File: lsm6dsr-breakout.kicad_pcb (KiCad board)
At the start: 2 copper layers, 16.5 x 20.3 mm, 16 parts, among them CN1 AFC10-S04QCA-00, CN2 AFC10-S04QCA-00, J1 Conn_01x06_Pin, J2 Conn_01x04_Pin, U1 LSM6DSRTR

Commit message: beautify schematic
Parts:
- removed the R1 at (56.0, 46.2)
- removed the R1 at (60.3, 51.8)
- added R1: 2.2k, Resistor_SMD:R_0402_1005Metric, F.Cu at (56.4, 48.3)
- added R6: 2.2k, Resistor_SMD:R_0402_1005Metric, F.Cu at (56.1, 52.3)
- R2, R3, R4, R5: value 3.9k -> 2.2k
- moved R5 6.10 mm to (56.0, 46.2)
- moved R3 4.22 mm to (60.3, 51.8), turned to 180 degrees
- moved R4 3.98 mm to (58.2, 51.8), turned to 0 degrees
- moved R2 2.44 mm to (56.4, 50.3), turned to 90 degrees
- moved C2 0.13 mm to (61.1, 50.3)
- turned C1 to 90 degrees
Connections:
- C1 pad 1: GND -> VDD
- C1 pad 2: VDD -> GND
- R2 pad 2: /XDA -> /SDA
- R3 pad 1: /SDA -> VDD
- R3 pad 2: VDD -> /XCL
- R4 pad 1: /SCL -> VDD
- R4 pad 2: VDD -> /XDA
- R5 pad 2: /SDO -> /CS
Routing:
- net GND: track 2.99 -> 4.50 mm, vias 12 -> 11

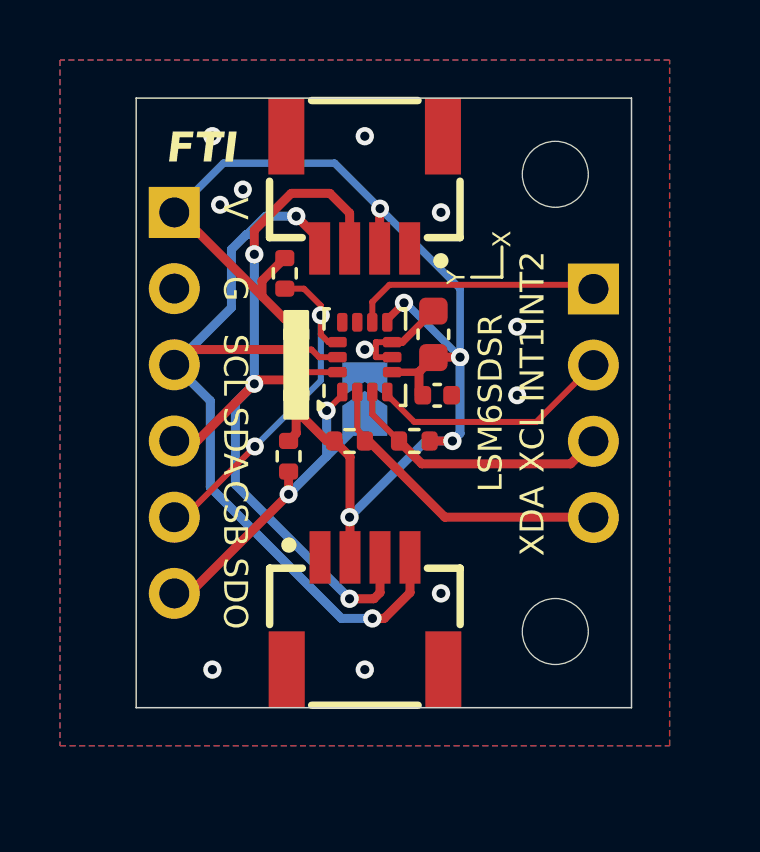
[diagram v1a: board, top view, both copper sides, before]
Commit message: use higher pullups, make it dippable, comply MEMS design guideline
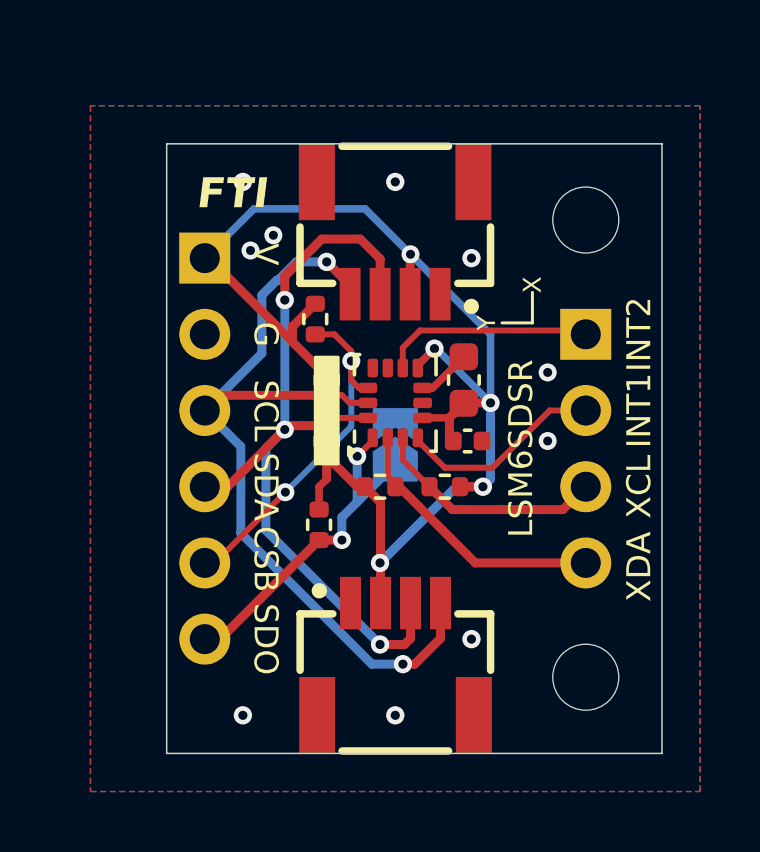
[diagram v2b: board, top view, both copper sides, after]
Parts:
- R1, R2, R3, R4, R5, R6: value 2.2k -> 4.7k
- moved R6 2.50 mm to (57.1, 54.6)
- moved CN1 1.83 mm to (59.7, 45.1)
- moved H1 1.83 mm to (66.0, 44.5)
- moved H2 1.83 mm to (66.0, 59.7)
- moved J1 1.83 mm to (53.3, 45.7)
- moved R1 1.83 mm to (57.4, 49.8)
- moved R2 1.83 mm to (57.4, 51.8)
- moved R4 1.83 mm to (59.2, 53.3)
- moved R5 1.83 mm to (57.0, 47.8)
- moved C1 1.83 mm to (62.0, 49.8)
- moved C2 1.83 mm to (62.1, 51.8)
- moved CN2 1.83 mm to (59.7, 59.1)
- moved JP1 1.83 mm to (59.7, 51.9)
- moved R3 1.83 mm to (61.3, 53.3)
- moved U1 1.83 mm to (59.7, 50.5)
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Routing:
- net GND: track 4.50 -> 2.59 mm, vias 11 -> 10
- net /XCL: track 9.01 -> 7.74 mm
- net /XDA: track 10.2 -> 8.96 mm
- net /INT1: track 8.03 -> 6.76 mm
- net /INT2: track 8.24 -> 6.97 mm
- net VDD: track 45.2 -> 46.0 mm
